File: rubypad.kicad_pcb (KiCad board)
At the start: 2 copper layers, 13 parts, among them U1 ProMicro

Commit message: Update - ran traces
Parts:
- added D7: D_Small, Keebio-Parts:Diode-dual, F.Cu at (67.5, 47.6)
- added G***: LOGO, rubypad-footprints:logo, F.Cu at (40.9, 27.4)
- added SW1: RotaryEncoder_Switch, Keebio-Parts:RotaryEncoder_EC11, F.Cu at (67.5, 34.9)
- moved MX6 51.5 mm to (86.5, 83.3)
- moved MX4 43.9 mm to (48.4, 83.3)
- moved D6 42.6 mm to (86.7, 89.7), turned to 180 degrees
- moved MX1 41.1 mm to (48.4, 64.3)
- moved D3 37.9 mm to (86.3, 70.6), turned to 180 degrees
- moved D5 37.0 mm to (67.5, 89.7), turned to 180 degrees
- moved MX2 36.9 mm to (67.5, 64.3)
- moved U1 32.1 mm to (84.9, 36.5), turned to -90 degrees
- moved MX3 30.4 mm to (86.5, 64.3)
- moved D2 29.6 mm to (67.3, 70.6), turned to 180 degrees
- moved MX5 26.9 mm to (67.5, 83.3)
- moved D4 20.1 mm to (48.5, 89.7), turned to 180 degrees
- moved D1 10.5 mm to (48.5, 70.6), turned to 180 degrees
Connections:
- D1 pad 1: row0 -> row1
- D2 pad 1: row0 -> row1
- D3 pad 1: row0 -> row1
- D4 pad 1: row1 -> row2
- D5 pad 1: row1 -> row2
- D6 pad 1: row1 -> row2
- U1 pad 10: unconnected-(U1-Pad10) -> row0
- U1 pad 11: unconnected-(U1-Pad11) -> row2
- U1 pad 12: unconnected-(U1-Pad12) -> row1
- U1 pad 13: unconnected-(U1-Pad13) -> ENCB
- U1 pad 14: unconnected-(U1-Pad14) -> ENCC
- U1 pad 15: unconnected-(U1-Pad15) -> ENCA
- U1 pad 7: unconnected-(U1-Pad7) -> col0
- U1 pad 8: unconnected-(U1-Pad8) -> col1
- U1 pad 9: unconnected-(U1-Pad9) -> col2
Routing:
- net row2: track 0.00 -> 111.5 mm
- net row1: track 0.00 -> 89.9 mm
- net ENCB: track 0.00 -> 63.3 mm
- net col0: track 0.00 -> 60.9 mm
- net ENCC: track 0.00 -> 57.1 mm
- net col1: track 0.00 -> 52.2 mm
- net ENCA: track 0.00 -> 50.8 mm
- net col2: track 0.00 -> 36.5 mm
- net row0: track 0.00 -> 18.8 mm
- net Net-(D3-Pad2): track 0.00 -> 12.3 mm
- net Net-(D2-Pad2): track 0.00 -> 12.3 mm
- net Net-(D5-Pad2): track 0.00 -> 12.2 mm
- net Net-(D1-Pad2): track 0.00 -> 12.2 mm
- net Net-(D4-Pad2): track 0.00 -> 12.2 mm
- net Net-(D6-Pad2): track 0.00 -> 12.1 mm
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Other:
- board outline added: 57.9 x 74.6 mm

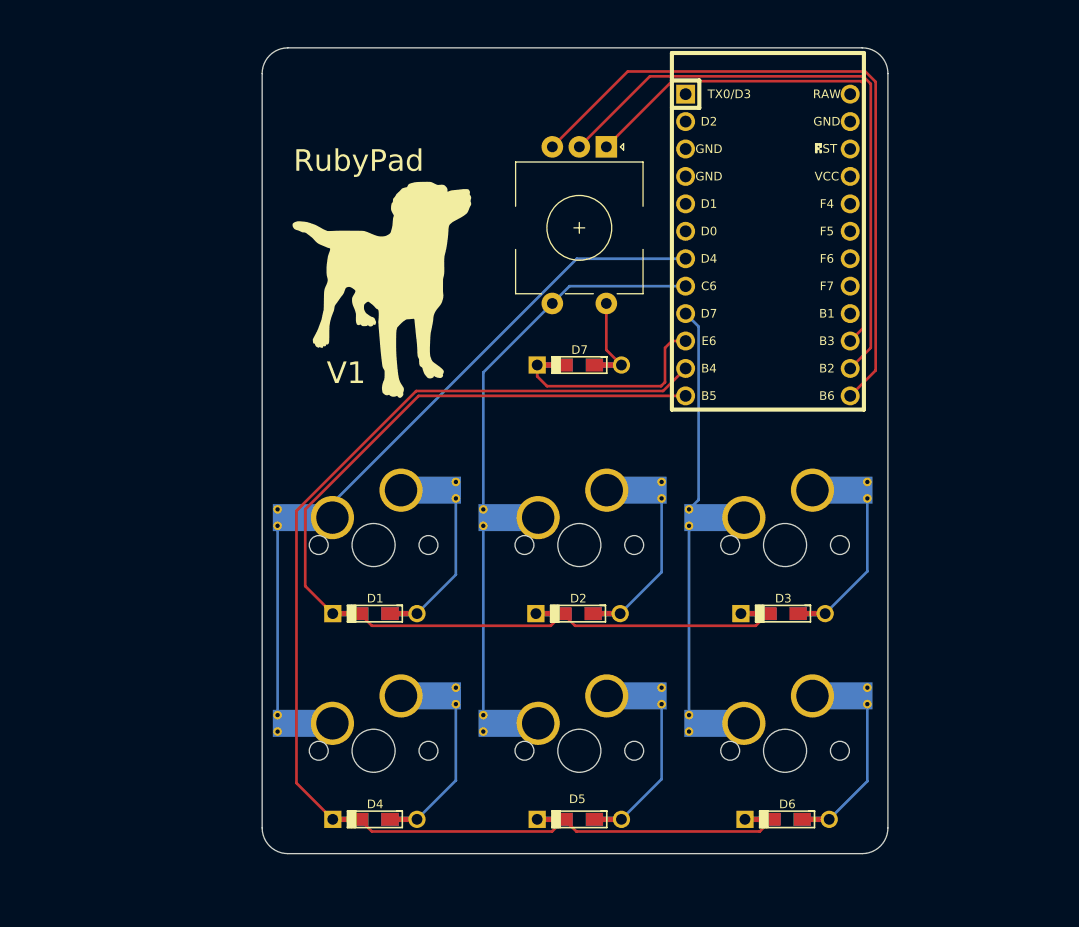
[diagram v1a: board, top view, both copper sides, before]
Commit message: Added 3d models
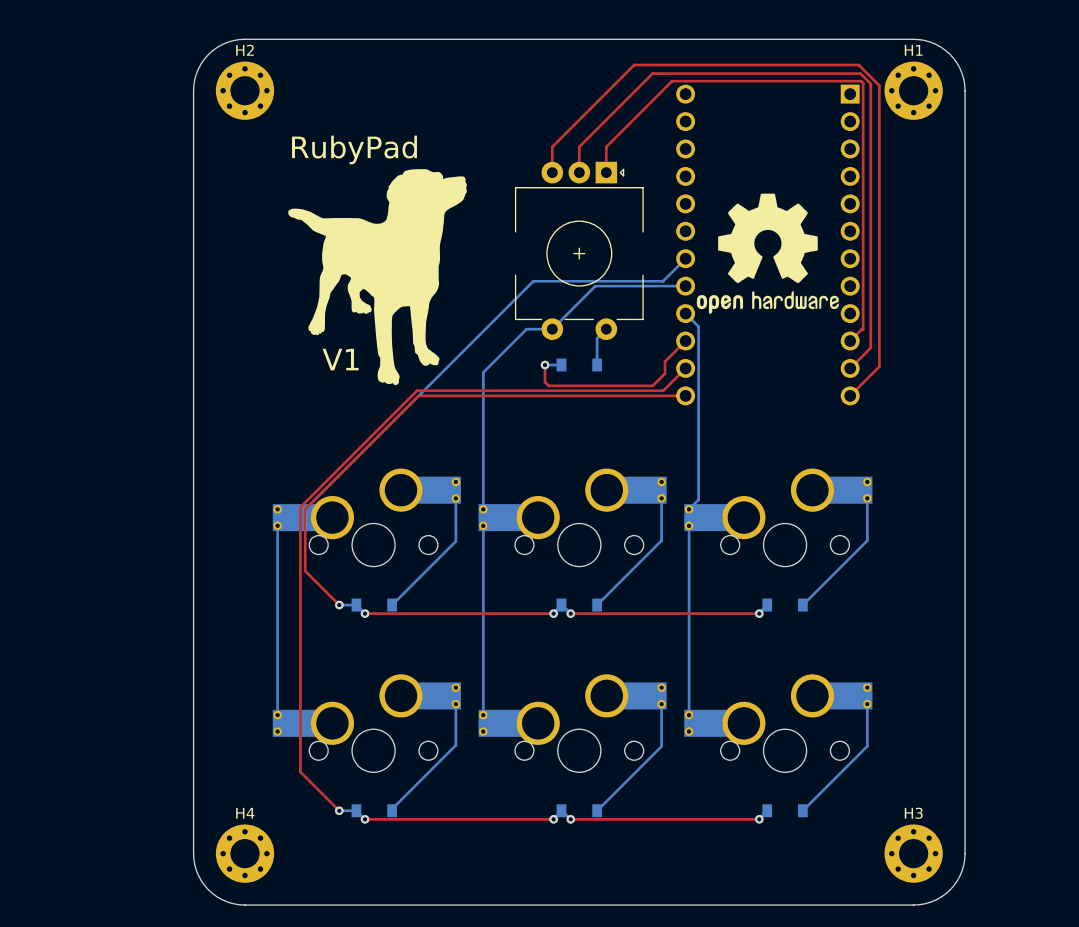
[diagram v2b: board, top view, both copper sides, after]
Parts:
- added H1: MountingHole, MountingHole:MountingHole_2.7mm_Pad_Via, F.Cu at (98.4, 22.2)
- added H2: MountingHole, MountingHole:MountingHole_2.7mm_Pad_Via, F.Cu at (36.5, 22.2)
- added H3: MountingHole, MountingHole:MountingHole_2.7mm_Pad_Via, F.Cu at (98.4, 92.9)
- added H4: MountingHole, MountingHole:MountingHole_2.7mm_Pad_Via, F.Cu at (36.5, 92.9)
- added REF**: OSHW-Logo2_14.6x12mm_SilkScreen, Symbol:OSHW-Logo2_14.6x12mm_SilkScreen, F.Cu at (84.9, 37.3)
- D1, D2, D3, D4, D5, D6, D7: footprint Keebio-Parts:Diode-dual -> Diode_SMD:D_SOD-123; moved to B.Cu
- U1: moved to B.Cu
- moved SW1 2.38 mm to (67.5, 37.3)
- moved G*** 1.24 mm to (40.5, 26.2)
- moved D3 0.82 mm to (86.5, 69.8), turned to 0 degrees
- moved D6 0.82 mm to (86.5, 88.9), turned to 0 degrees
- moved D2 0.80 mm to (67.5, 69.8), turned to 0 degrees
- moved D1 0.80 mm to (48.5, 69.8), turned to 0 degrees
- moved D4 0.80 mm to (48.5, 88.9), turned to 0 degrees
- moved D5 0.79 mm to (67.5, 88.9), turned to 0 degrees
- turned D7 to 0 degrees
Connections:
- U1 pad 10: row0 -> ENCA
- U1 pad 11: row2 -> ENCC
- U1 pad 12: row1 -> ENCB
- U1 pad 13: ENCB -> row1
- U1 pad 14: ENCC -> row2
- U1 pad 15: ENCA -> row0
- U1 pad 16: unconnected-(U1-Pad16) -> col2
- U1 pad 17: unconnected-(U1-Pad17) -> col1
- U1 pad 18: unconnected-(U1-Pad18) -> col0
- U1 pad 7: col0 -> unconnected-(U1-Pad7)
- U1 pad 8: col1 -> unconnected-(U1-Pad8)
- U1 pad 9: col2 -> unconnected-(U1-Pad9)
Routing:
- net col0: track 60.9 -> 64.8 mm
- net ENCB: track 63.3 -> 66.4 mm
- net Net-(D7-Pad2): track 6.28 -> 3.67 mm
- net ENCC: track 57.1 -> 59.7 mm
- net ENCA: track 50.8 -> 53.2 mm
- net row1: track 89.9 -> 90.8 mm, vias 0 -> 5
- net row0: track 18.8 -> 18.6 mm, vias 0 -> 1
- net row2: track 111.5 -> 111.6 mm, vias 0 -> 5
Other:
- board size 57.9 x 74.6 mm -> 71.4 x 80.2 mm

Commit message: update
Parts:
- removed REF**: OSHW-Logo2_14.6x12mm_SilkScreen, Symbol:OSHW-Logo2_14.6x12mm_SilkScreen
- added G***: LOGO, rubypad-footprints:qmk-22mm, F.Cu at (32.5, 48.4)
- moved G*** 16.7 mm to (24.6, 21.0)
- moved H2 16.0 mm to (20.6, 20.6)
- moved H4 16.0 mm to (20.6, 91.3)
- moved D1 16.0 mm to (32.6, 68.3)
- moved D2 16.0 mm to (51.6, 68.3)
- moved D3 16.0 mm to (70.6, 68.3)
- moved D4 16.0 mm to (32.6, 87.3)
- moved D5 16.0 mm to (51.6, 87.3)
- moved D6 16.0 mm to (70.6, 87.3)
- moved D7 16.0 mm to (51.6, 46.0)
- moved H1 16.0 mm to (82.5, 20.6)
- moved H3 16.0 mm to (82.5, 91.3)
- moved MX1 16.0 mm to (32.5, 62.7)
- moved MX2 16.0 mm to (51.6, 62.7)
- moved MX3 16.0 mm to (70.6, 62.7)
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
